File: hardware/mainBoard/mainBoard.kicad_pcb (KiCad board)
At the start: 2 copper layers, 99.9 x 52.5 mm, 25 parts, among them J1 UARTDebug, J2 LeftKeyConnector, J3 DisplayConnector, J4 LEDHeader, J5 RightKeyConnector, J6 EncoderConnector, U1 MCP4728-E_UN

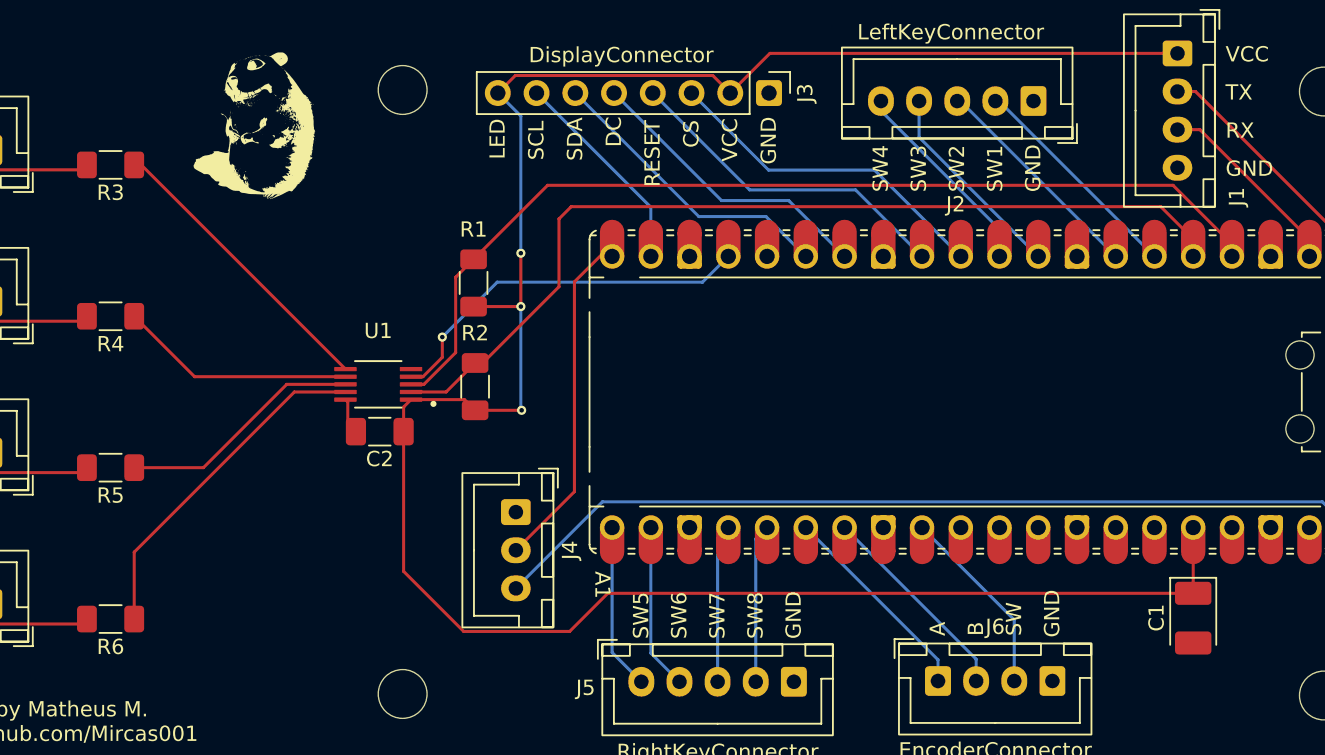
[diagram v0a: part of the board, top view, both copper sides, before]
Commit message: update mainboard to use resistor array
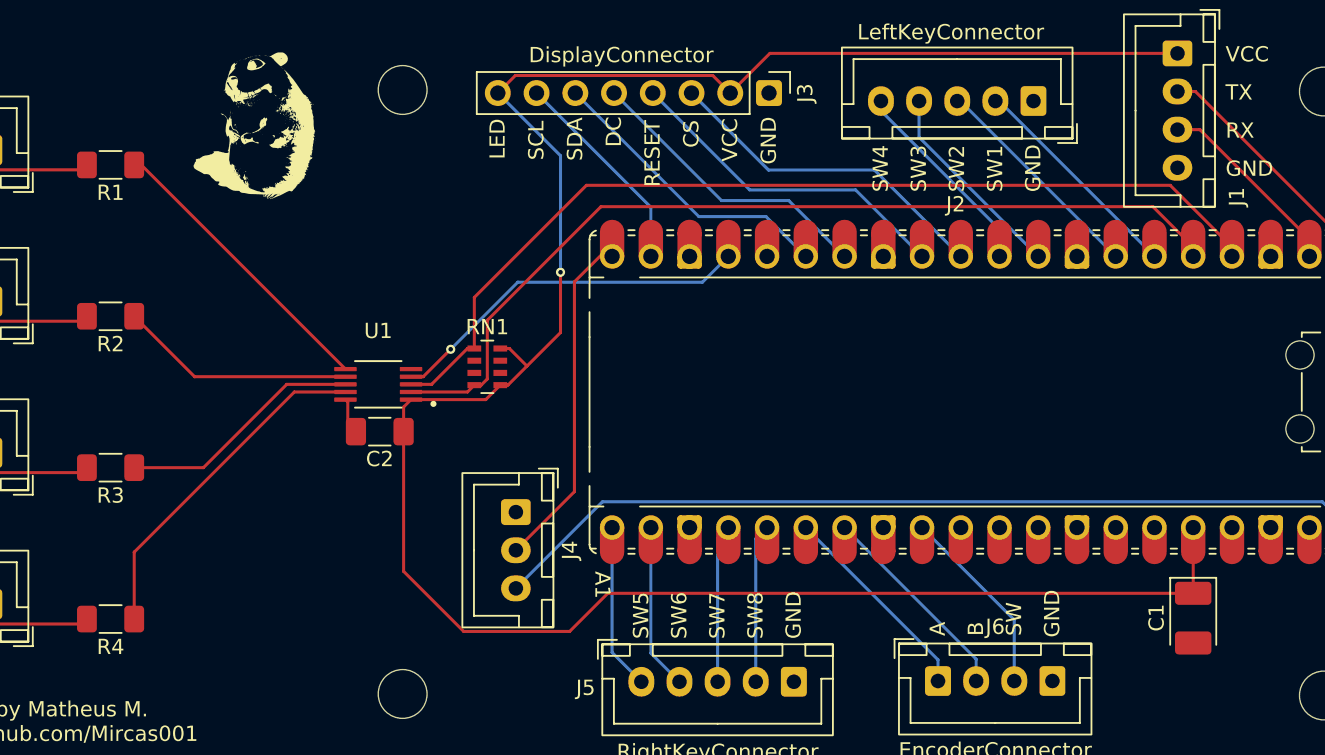
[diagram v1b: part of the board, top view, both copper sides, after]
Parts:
- removed the R1 at (148.2, 87.8)
- removed the R2 at (148.3, 94.7)
- added RN1: R_Pack04, Resistor_SMD:R_Array_Concave_4x0603, F.Cu at (149.2, 93.3)
- renumbered R3 to R1, R4 to R2, R5 to R3, R6 to R4
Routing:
- net +3V3: track 149.0 -> 148.1 mm, vias 3 -> 1
- net /LDAC: track 24.8 -> 24.1 mm

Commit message: update BOM to change capacitor + new gerbers + update the production files
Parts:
- RN1: value R_Pack04 -> 10K
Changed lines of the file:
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@@
 			)
 		)
-		(property "Value" "R_Pack04"
+		(property "Value" "10K"
 			(at 0 2.6 0)
 			(layer "F.Fab")
@@
 			)
 		)
+		(property "LCSC Part #" "C29718"
+			(at 0 0 0)
+			(unlocked yes)
+			(layer "F.Fab")
+			(hide yes)
+			(effects
+				(font
+					(size 1 1)
+					(thickness 0.15)
+				)
+			)
+		)
+		(property "Price" " $0.0149 "
+			(at 0 0 0)
+			(unlocked yes)
+			(layer "F.Fab")
+			(hide yes)
+			(effects
+				(font
+					(size 1 1)
+					(thickness 0.15)
+				)
+			)
+		)
 		(property ki_fp_filters "DIP* SOIC* R*Array*Concave* R*Array*Convex* MSOP*")
 		(sheetname "/")
@@
 			(net "unconnected-(RN1-R2.1-Pad2)")
 			(pinfunction "R2.1_2")
-			(pintype "passive")
+			(pintype "passive+no_connect")
 		)
 		(pad "3" smd rect
@@
 			(net "unconnected-(RN1-R3.1-Pad3)")
 			(pinfunction "R3.1_3")
-			(pintype "passive")
+			(pintype "passive+no_connect")
 		)
 		(pad "4" smd rect
@@
 			(net "unconnected-(RN1-R3.2-Pad6)")
 			(pinfunction "R3.2_6")
-			(pintype "passive")
+			(pintype "passive+no_connect")
 		)
 		(pad "7" smd rect
@@
 			(net "unconnected-(RN1-R2.2-Pad7)")
 			(pinfunction "R2.2_7")
-			(pintype "passive")
+			(pintype "passive+no_connect")
 		)
 		(pad "8" smd rect
@@
 			(net "unconnected-(A1-GPIO26_ADC0-Pad31)")
 			(pinfunction "GPIO26_ADC0_31")
-			(pintype "bidirectional")
+			(pintype "bidirectional+no_connect")
 		)
 		(pad "31" smd roundrect
@@
 			(layers "F.Cu" "F.Mask")
 			(roundrect_rratio 0.5)
-			(net "unconnected-(A1-GPIO26_ADC0-Pad31)")
+			(net "unconnected-(A1-GPIO26_ADC0-Pad31)_1")
 			(pinfunction "GPIO26_ADC0_31")
-			(pintype "bidirectional")
+			(pintype "bidirectional+no_connect")
 		)
 		(pad "32" thru_hole circle
@@
 			)
 		)
-		(property "LCSC Part #" "C1952719"
+		(property "LCSC Part #" "C1958016"
 			(at 0 0 270)
 			(unlocked yes)
@@
 			)
 		)
-		(property "Price" " $0.716 "
+		(property "Price" "$ 0.2239"
 			(at 0 0 270)
 			(unlocked yes)
